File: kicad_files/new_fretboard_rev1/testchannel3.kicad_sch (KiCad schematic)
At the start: 22 parts, among them U2 LX3302AQPW-TR-EASY

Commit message: got 6 of em
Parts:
- removed C12, C13: 680pf, Capacitor_SMD:C_0603_1608Metric, symbol Device:C
- removed C14, C15: 10pf, Capacitor_SMD:C_0402_1005Metric, symbol Device:C
- removed C16: 1uf, Capacitor_SMD:C_0603_1608Metric, symbol Device:C
- removed C17, C20: 100nf, Capacitor_SMD:C_0402_1005Metric, symbol Device:C
- removed C18, C19: 6.8nf, Capacitor_SMD:C_0402_1005Metric, symbol Device:C
- removed C21: 1000pf, Capacitor_SMD:C_0402_1005Metric, symbol Device:C
- removed C22: 470nf, Capacitor_SMD:C_0402_1005Metric, symbol Device:C
- removed L5, L6, L7, L8: L, NetTie:NetTie-2_SMD_Pad0.5mm, symbol Device:L
- removed R10, R11, R8, R9: 10R, Resistor_SMD:R_0402_1005Metric, symbol Device:R
- removed R12: 221R, Resistor_SMD:R_0402_1005Metric, symbol Device:R
- removed R13: 4.7R, Resistor_SMD:R_0402_1005Metric, symbol Device:R
- removed U2: LX3302AQPW-TR-EASY, Snapeda:14-TSSOP_MCH-L, symbol Snapeda:LX3302AQPW-TR-EASY
- added C34, C40: 100nf, Capacitor_SMD:C_0402_1005Metric, symbol Device:C
- added C35: 1000pf, Capacitor_SMD:C_0402_1005Metric, symbol Device:C
- added C36: 470nf, Capacitor_SMD:C_0402_1005Metric, symbol Device:C
- added C37: 1uf, Capacitor_SMD:C_0603_1608Metric, symbol Device:C
- added C38, C39: 6.8nf, Capacitor_SMD:C_0402_1005Metric, symbol Device:C
- added C41, C42: 10pf, Capacitor_SMD:C_0402_1005Metric, symbol Device:C
- added C43, C44: 680pf, Capacitor_SMD:C_0603_1608Metric, symbol Device:C
- added L13, L14, L15, L16: L, NetTie:NetTie-2_SMD_Pad0.5mm, symbol Device:L
- added R19: 4.7R, Resistor_SMD:R_0402_1005Metric, symbol Device:R
- added R20: 221R, Resistor_SMD:R_0402_1005Metric, symbol Device:R
- added R21, R22, R23, R24: 10R, Resistor_SMD:R_0402_1005Metric, symbol Device:R
- added U4: LX3302AQPW-TR-EASY, Snapeda:14-TSSOP_MCH-L, symbol Snapeda:LX3302AQPW-TR-EASY
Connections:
- net CL1B_A: now also L16.1, R24.2
- net CL1_A: now also C41.1, R24.1, U4.8 (CL1)
- net CL2B_A: now also L15.1, R23.2
- net CL2_A: now also C42.1, R23.1, U4.10 (CL2)
- net GND: now also C34.1, C35.1, C36.1, C37.1, C38.1, C39.1, C41.2, C42.2, C43.2, C44.2, L15.2, L16.2, U4.2 (GND), U4.9 (GNDCL)
- net OSC11_A: now also C43.1, L13.2, U4.13 (OSC1)
- net OSC12_A: now also C44.1, L14.2, U4.12 (OSC2)
- net SUB_A: now also C40.1, U4.11 (SUB)
- net VIN_A: now also C35.2, C36.2, R19.1, R21.2, R22.1, U4.4 (VIN)
- new net: C37.2, C40.2, U4.5 (VDD)
- new net: C39.2, R20.1, R21.1, U4.6 (IO2)
- new net: C34.2, R19.2
- new net: C38.2, R20.2
- new net /OSC2B_A: L13.1, L14.1, R22.2
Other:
- removed sheet testchannel1
- removed sheet testchannel2
- removed sheet testchannel3
- removed sheet testchannel4
- removed sheet testchannel5

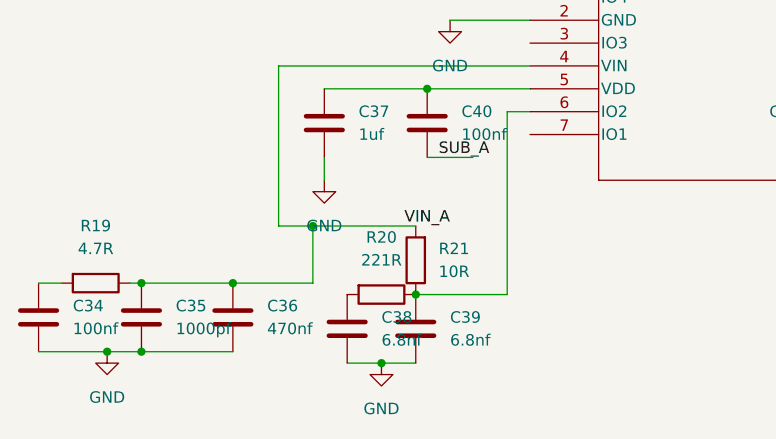
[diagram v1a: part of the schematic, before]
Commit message: stm32 micro added
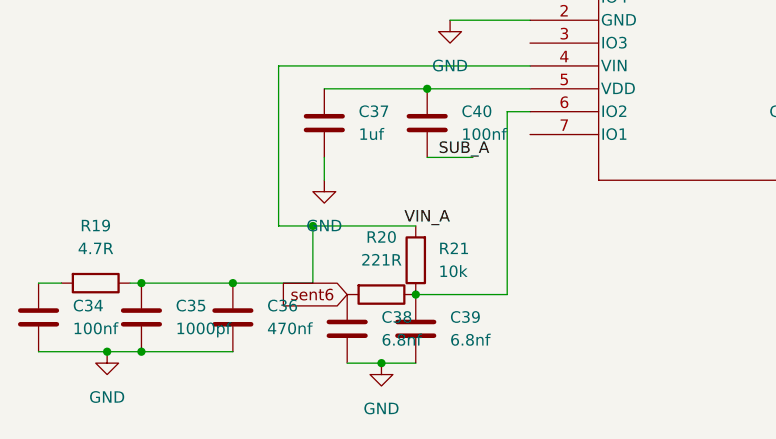
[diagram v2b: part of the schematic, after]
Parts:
- R21: value 10R -> 10k
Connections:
- net sent6: now reaches C38.2, R20.2
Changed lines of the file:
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@@
+		)
+	)
+	(global_label "sent6"
+		(shape input)
+		(at 91.44 118.11 180)
+		(fields_autoplaced yes)
+		(effects
+			(font
+				(size 1.27 1.27)
+			)
+			(justify right)
+		)
+		(property "Intersheetrefs" "${INTERSHEET_REFS}"
+			(at 83.2539 118.11 0)
+			(effects
+				(font
+					(size 1.27 1.27)
+				)
+				(justify right)
+				(hide yes)
+			)
 		)
 	)
@@
 			)
 		)
-		(property "Component Class" ""
-			(at 171.45 105.41 90)
-			(effects
-				(font
-					(size 1.27 1.27)
-				)
-				(hide yes)
-			)
-		)
 		(pin "2"
 		)
@@
 			)
 		)
-		(property "Component Class" ""
-			(at 165.1 49.53 0)
-			(effects
-				(font
-					(size 1.27 1.27)
-				)
-				(hide yes)
-			)
-		)
 		(pin "2"
 		)
@@
 			)
 		)
-		(property "Component Class" ""
-			(at 185.42 90.17 90)
-			(effects
-				(font
-					(size 1.27 1.27)
-				)
-				(hide yes)
-			)
-		)
 		(pin "1"
 		)
@@
 			)
 		)
-		(property "Component Class" ""
-			(at 68.58 120.65 0)
-			(effects
-				(font
-					(size 1.27 1.27)
-				)
-				(hide yes)
-			)
-		)
 		(pin "1"
 		)
@@
 			)
 		)
-		(property "Component Class" ""
-			(at 165.1 60.96 0)
-			(effects
-				(font
-					(size 1.27 1.27)
-				)
-				(hide yes)
-			)
-		)
 		(pin "1"
 		)
@@
 			)
 		)
-		(property "Component Class" ""
-			(at 88.9 99.06 0)
-			(effects
-				(font
-					(size 1.27 1.27)
-				)
-				(hide yes)
-			)
-		)
 		(pin "1"
 		)
@@
 			)
 		)
-		(property "Component Class" ""
-			(at 111.76 85.09 0)
-			(effects
-				(font
-					(size 1.27 1.27)
-				)
-				(hide yes)
-			)
-		)
 		(pin "5"
 		)
@@
 			)
 		)
-		(property "Component Class" ""
-			(at 172.72 114.3 90)
-			(effects
-				(font
-					(size 1.27 1.27)
-				)
-				(hide yes)
-			)
-		)
 		(pin "2"
 		)
@@
 			)
 		)
-		(property "Component Class" ""
-			(at 63.5 116.84 90)
-			(effects
-				(font
-					(size 1.27 1.27)
-				)
-				(hide yes)
-			)
-		)
 		(pin "2"
 		)
@@
 			)
 		)
-		(property "Component Class" ""
-			(at 184.15 105.41 90)
-			(effects
-				(font
-					(size 1.27 1.27)
-				)
-				(hide yes)
-			)
-		)
 		(pin "1"
 		)
@@
 			)
 		)
-		(property "Component Class" ""
-			(at 185.42 77.47 90)
-			(effects
-				(font
-					(size 1.27 1.27)
-				)
-				(hide yes)
-			)
-		)
 		(pin "1"
 		)
@@
 			)
 		)
-		(property "Component Class" ""
-			(at 57.15 120.65 0)
-			(effects
-				(font
-					(size 1.27 1.27)
-				)
-				(hide yes)
-			)
-		)
 		(pin "1"
 		)
@@
 			)
 		)
-		(property "Component Class" ""
-			(at 78.74 120.65 0)
-			(effects
-				(font
-					(size 1.27 1.27)
-				)
-				(hide yes)
-			)
-		)
 		(pin "1"
 		)
@@
 			)
 		)
-		(property "Component Class" ""
-			(at 99.06 121.92 0)
-			(effects
-				(font
-					(size 1.27 1.27)
-				)
-				(hide yes)
-			)
-		)
 		(pin "1"
 		)
@@
 			)
 		)
-		(property "Component Class" ""
-			(at 171.45 95.25 90)
-			(effects
-				(font
-					(size 1.27 1.27)
-				)
-				(hide yes)
-			)
-		)
 		(pin "1"
 		)
@@
 			)
 		)
-		(property "Component Class" ""
-			(at 184.15 114.3 90)
-			(effects
-				(font
-					(size 1.27 1.27)
-				)
-				(hide yes)
-			)
-		)
 		(pin "1"
 		)
@@
 			)
 		)
-		(property "Component Class" ""
-			(at 91.44 121.92 0)
-			(effects
-				(font
-					(size 1.27 1.27)
-				)
-				(hide yes)
-			)
-		)
 		(pin "1"
 		)
@@
 			)
 		)
-		(property "Component Class" ""
-			(at 100.33 99.06 0)
-			(effects
-				(font
-					(size 1.27 1.27)
-				)
-				(hide yes)
-			)
-		)
 		(pin "1"
 		)
@@
 			)
 		)
-		(property "Component Class" ""
-			(at 95.25 118.11 90)
-			(effects
-				(font
-					(size 1.27 1.27)
-				)
-				(hide yes)
-			)
-		)
 		(pin "2"
 		)
@@
 			)
 		)
-		(property "Component Class" ""
-			(at 170.18 125.73 90)
-			(effects
-				(font
-					(size 1.27 1.27)
-				)
-				(hide yes)
-			)
-		)
 		(pin "1"
 		)
@@
 			)
 		)
-		(property "Value" "10R"
+		(property "Value" "10k"
 			(at 101.6 115.5699 0)
 			(effects
@@
 			)
 		)
-		(property "Component Class" ""
-			(at 99.06 114.3 0)
-			(effects
-				(font
-					(size 1.27 1.27)
-				)
-				(hide yes)
-			)
-		)
 		(pin "2"
 		)
@@
 			(at 175.26 60.96 0)
 			(effects
-				(font
-					(size 1.27 1.27)
-				)
-				(hide yes)
-			)
-		)
-		(property "Component Class" ""
-			(at 175.26 60.96 0)
-			(effects

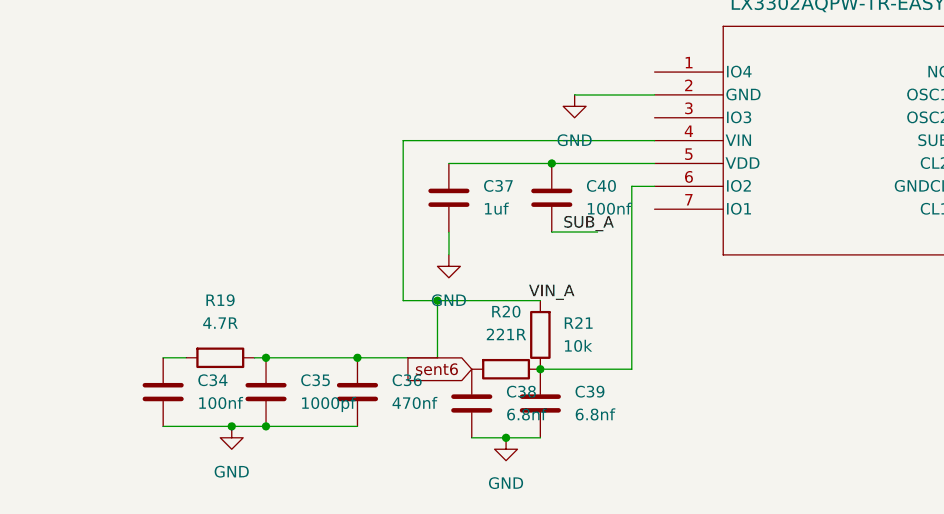
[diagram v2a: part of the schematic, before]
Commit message: mcu configured, still needs power connections and spi i2c connections
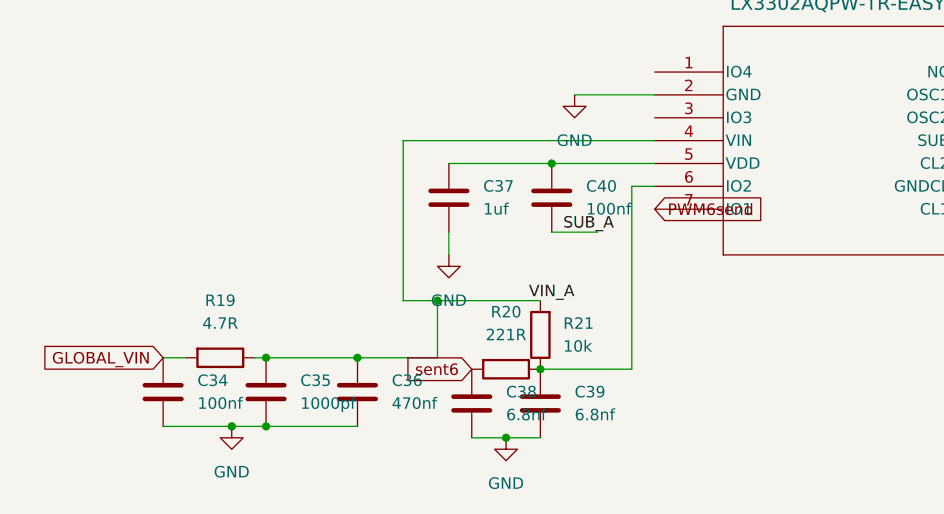
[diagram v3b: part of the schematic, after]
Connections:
- net PWM6send: now reaches U4.7 (IO1)
- net GLOBAL_VIN: now reaches C34.2, R19.2
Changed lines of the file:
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@@
+		)
+	)
+	(global_label "GLOBAL_VIN"
+		(shape input)
+		(at 57.15 116.84 180)
+		(fields_autoplaced yes)
+		(effects
+			(font
+				(size 1.27 1.27)
+			)
+			(justify right)
+		)
+		(property "Intersheetrefs" "${INTERSHEET_REFS}"
+			(at 43.158 116.84 0)
+			(effects
+				(font
+					(size 1.27 1.27)
+				)
+				(justify right)
+				(hide yes)
+			)
 		)
 	)
@@
 				(hide yes)
 			)
+		)
+	)
+	(global_label "PWM6send"
+		(shape input)
+		(at 111.76 100.33 0)
+		(fields_autoplaced yes)
+		(effects
+			(font
+				(size 1.27 1.27)
+			)
+			(justify left)
+		)
+		(property "Intersheetrefs" "${INTERSHEET_REFS}"
+			(at 124.5422 100.33 0)
+			(effects
+				(font
+					(size 1.27 1.27)
+				)
+				(justify left)
+				(hide yes)
+			)

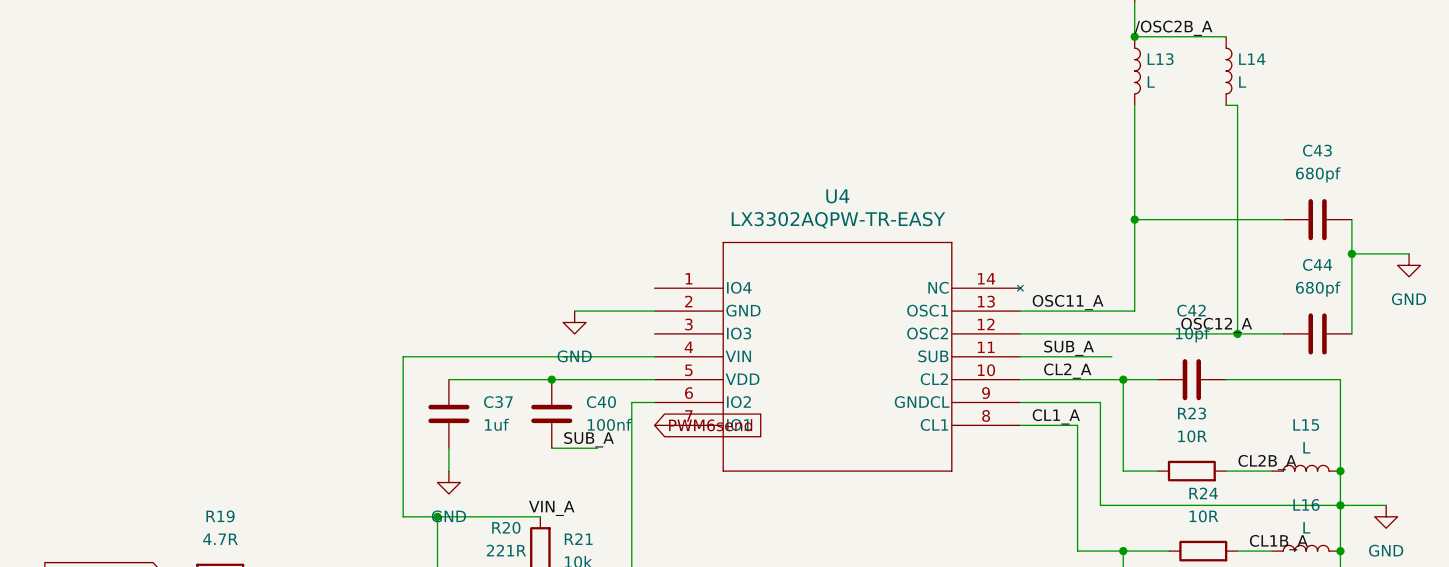
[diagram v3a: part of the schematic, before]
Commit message: finished routing - adding silkscreen
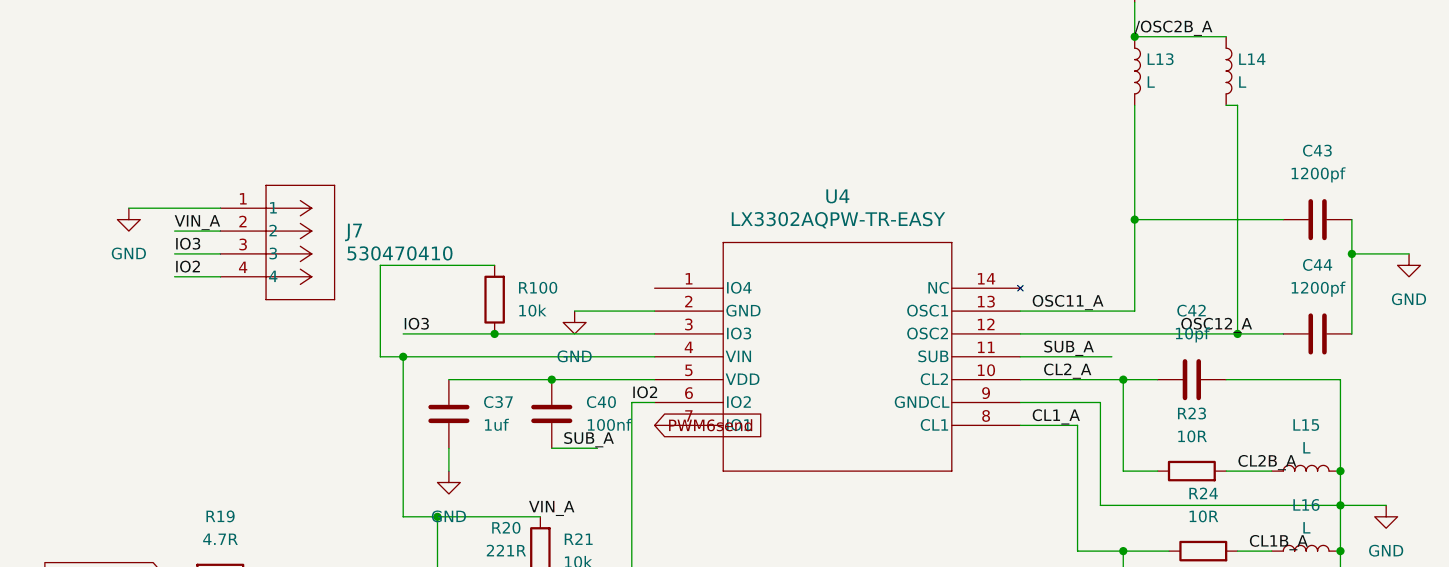
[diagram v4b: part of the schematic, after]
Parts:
- added J7: 530470410, Snapeda:CONN04_530470410_MOL, symbol Snapeda:530470410
- added R100: 10k, Resistor_SMD:R_0402_1005Metric, symbol Device:R
- C43, C44: value 680pf -> 1200pf
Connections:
- net GND: now also J7.1
- net VIN_A: now also J7.2, R100.2
- net IO3: now reaches U4.3 (IO3)
- net IO3: now also J7.3, R100.1
- net IO2: now reaches C39.2, R20.1, R21.1, U4.6 (IO2)
- net IO2: now also J7.4

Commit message: exported gerbers of lefthand
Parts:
- L13, L14, L15, L16: now left out of the parts list
